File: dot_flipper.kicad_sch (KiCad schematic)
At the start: 54 parts, among them J1 INPUT, J2 OUTPUT, J3 Conn_01x06_Socket, J4 Conn_01x06_Socket, U1 SN74LVC1G04DCKR, U10 SN74LVC1G04DCKR, U11 DRV8837CDSGR, U12 CDSOT236-T05C, U13 SN74LVC1G04DCKR, U14 DRV8837CDSGR, U15 SN74LVC1G04DCKR, U16 DRV8837CDSGR, U17 SN74LVC1G04DCKR, U18 DRV8837CDSGR, U2 DRV8837CDSGR, U3 7_flip_dots, U4 SN74HC595PWR, U5 SN74LVC1G04DCKR, U6 DRV8837CDSGR, U7 SN74LVC1G04DCKR, U8 DRV8837CDSGR, U9 CDSOT236-T05C

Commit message: Power supply mod
Connected VM to VCC to simplify operation and make PCB layout easier
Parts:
- removed C1, C11, C14, C17, C20, C5, C8: 100n/16V, Capacitor_SMD:C_0201_0603Metric_Pad0.64x0.40mm_HandSolder, symbol Device:C
- removed J1: INPUT, symbol Connector:Conn_01x07_Pin
- removed J2: OUTPUT, symbol Connector:Conn_01x07_Socket
- removed J3: Conn_01x06_Socket, Connector_JST:JST_XH_S6B-XH-A-1_1x06_P2.50mm_Horizontal, symbol Connector:Conn_01x06_Socket
- removed J4: Conn_01x06_Socket, Connector_PinSocket_2.54mm:PinSocket_1x06_P2.54mm_Vertical, symbol Connector:Conn_01x06_Socket
- removed JP1: SolderJumper_2_Open, Jumper:SolderJumper-2_P1.3mm_Open_RoundedPad1.0x1.5mm, symbol Jumper:SolderJumper_2_Open
- removed TP9: SEROUT2, TestPoint:TestPoint_Pad_D1.5mm, symbol Connector:TestPoint
- removed U12: CDSOT236-T05C, Package_TO_SOT_SMD:SOT-23-6, symbol Power_Protection:CDSOT236-0504C
- added FID1, FID2: Fiducial, symbol Mechanical:Fiducial
- added H1, H2: MountingHole_Pad, MountingHole:MountingHole_2.2mm_M2_Pad_Via, symbol Mechanical:MountingHole_Pad
- added J1: VCC_i, Connector_Wire:SolderWirePad_1x01_SMD_1x2mm, symbol Connector:Conn_01x01_Pin
- added J10: LATCH_o, Connector_Wire:SolderWirePad_1x01_SMD_1x2mm, symbol Connector:Conn_01x01_Pin
- added J11: SLEEP_o, Connector_Wire:SolderWirePad_1x01_SMD_1x2mm, symbol Connector:Conn_01x01_Pin
- added J12: GND_o, Connector_Wire:SolderWirePad_1x01_SMD_1x2mm, symbol Connector:Conn_01x01_Pin
- added J2: SERIN, Connector_Wire:SolderWirePad_1x01_SMD_1x2mm, symbol Connector:Conn_01x01_Pin
- added J3: SRCLK_i, Connector_Wire:SolderWirePad_1x01_SMD_1x2mm, symbol Connector:Conn_01x01_Pin
- added J4: LATCH_i, Connector_Wire:SolderWirePad_1x01_SMD_1x2mm, symbol Connector:Conn_01x01_Pin
- added J5: SLEEP_i, Connector_Wire:SolderWirePad_1x01_SMD_1x2mm, symbol Connector:Conn_01x01_Pin
- added J6: GND_i, Connector_Wire:SolderWirePad_1x01_SMD_1x2mm, symbol Connector:Conn_01x01_Pin
- added J7: VCC_o, Connector_Wire:SolderWirePad_1x01_SMD_1x2mm, symbol Connector:Conn_01x01_Pin
- added J8: SEROUT, Connector_Wire:SolderWirePad_1x01_SMD_1x2mm, symbol Connector:Conn_01x01_Pin
- added J9: SRCLK_o, Connector_Wire:SolderWirePad_1x01_SMD_1x2mm, symbol Connector:Conn_01x01_Pin
- TP1: value SEROUT1 -> SEROUT
- renumbered C2 to C1, C15 to C10, C16 to C11, C18 to C12, C19 to C13, C21 to C14, C22 to C15, C3 to C2, C4 to C3, C6 to C4, C7 to C5, C9 to C6, C10 to C7, C12 to C8, C13 to C9, U13 to U12, U14 to U13, U15 to U14, U16 to U15, U17 to U16, U18 to U17
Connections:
- net GND: now also H1.1, H2.1, J12.1 (Pin_1), J6.1 (Pin_1)
- net LATCH: now also J10.1 (Pin_1), J4.1 (Pin_1)
- net SERIN: now also U9.6 (IO4), J2.1 (Pin_1); no longer U9.1 (IO1)
- net SLEEP: now also U9.3 (IO2), J11.1 (Pin_1), J5.1 (Pin_1); no longer U9.6 (IO4)
- net SRCLK: now also U9.5 (VP), J3.1 (Pin_1), J9.1 (Pin_1); no longer U9.3 (IO2)
- net VCC: now also C1.1, C10.1, C11.1, C12.1, C13.1, C14.1, C15.1, C2.1, C4.1, C5.1, C6.1, C7.1, C8.1, C9.1, U11.1 (VM), U13.1 (VM), U15.1 (VM), U17.1 (VM), U2.1 (VM), U6.1 (VM), U8.1 (VM), U9.1 (IO1), J1.1 (Pin_1), J7.1 (Pin_1); no longer U9.5 (VP)
- net VM: no longer C1.1, C10.1, C11.1, C12.1, C13.1, C14.1, C15.1, C2.1, C4.1, C5.1, C6.1, C7.1, C8.1, C9.1, U11.1 (VM), U13.1 (VM), U15.1 (VM), U17.1 (VM), U2.1 (VM), U6.1 (VM), U8.1 (VM)
- net SEROUT1 renamed SEROUT
- net SEROUT: now also J8.1 (Pin_1)

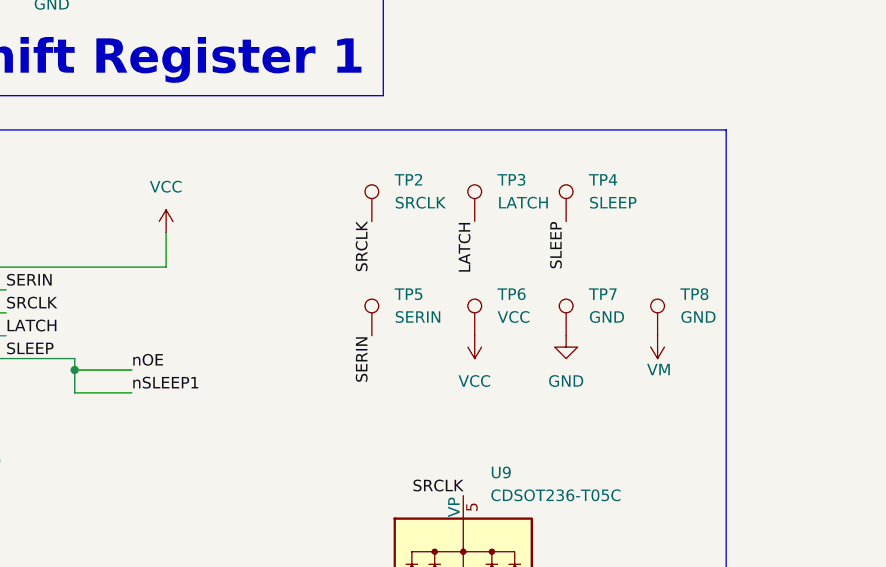
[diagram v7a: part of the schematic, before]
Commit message: Started PCB layout
Components in vaguely the correct area
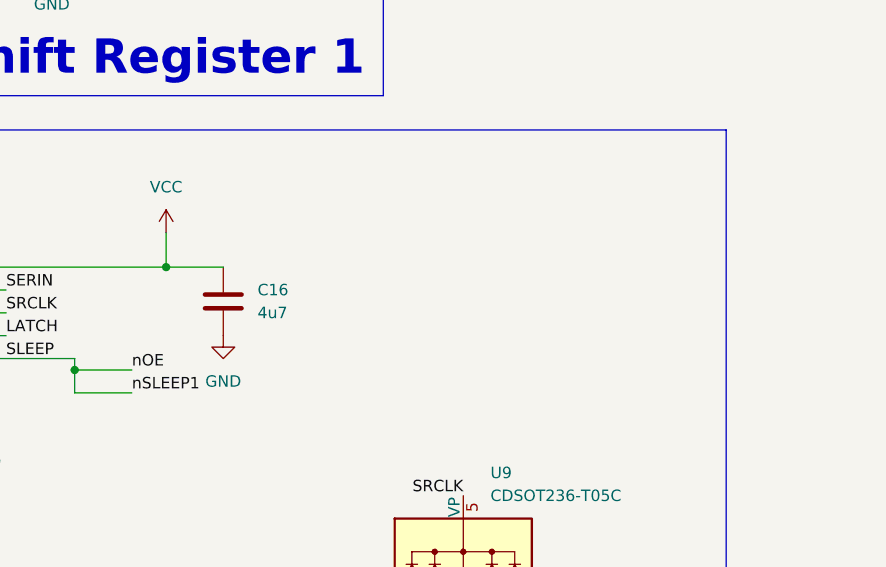
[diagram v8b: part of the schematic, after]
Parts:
- removed TP2: SRCLK, TestPoint:TestPoint_Pad_D1.5mm, symbol Connector:TestPoint
- removed TP3: LATCH, TestPoint:TestPoint_Pad_D1.5mm, symbol Connector:TestPoint
- removed TP4: SLEEP, TestPoint:TestPoint_Pad_D1.5mm, symbol Connector:TestPoint
- removed TP5: SERIN, TestPoint:TestPoint_Pad_D1.5mm, symbol Connector:TestPoint
- removed TP6: VCC, TestPoint:TestPoint_Pad_D1.5mm, symbol Connector:TestPoint
- removed TP7, TP8: GND, TestPoint:TestPoint_Pad_D1.5mm, symbol Connector:TestPoint
- added C16: 4u7, Capacitor_SMD:C_0805_2012Metric, symbol Device:C
- C1, C10, C11, C12, C13, C14, C15, C2, C3, C4, C5, C6, C7, C8, C9: footprint Capacitor_SMD:C_0201_0603Metric_Pad0.64x0.40mm_HandSolder -> Capacitor_SMD:C_0603_1608Metric
- FID1, FID2: footprint (none) -> Fiducial:Fiducial_0.5mm_Mask1.5mm
- TP1: footprint TestPoint:TestPoint_Pad_D1.5mm -> TestPoint:TestPoint_Pad_D1.0mm
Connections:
- net GND: now also C16.2
- net VCC: now also C16.1
